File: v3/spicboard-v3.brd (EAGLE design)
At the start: 100 x 80 mm, 39 parts, among them IC1 74HC595N, Q1 BC557, Q2 BC557

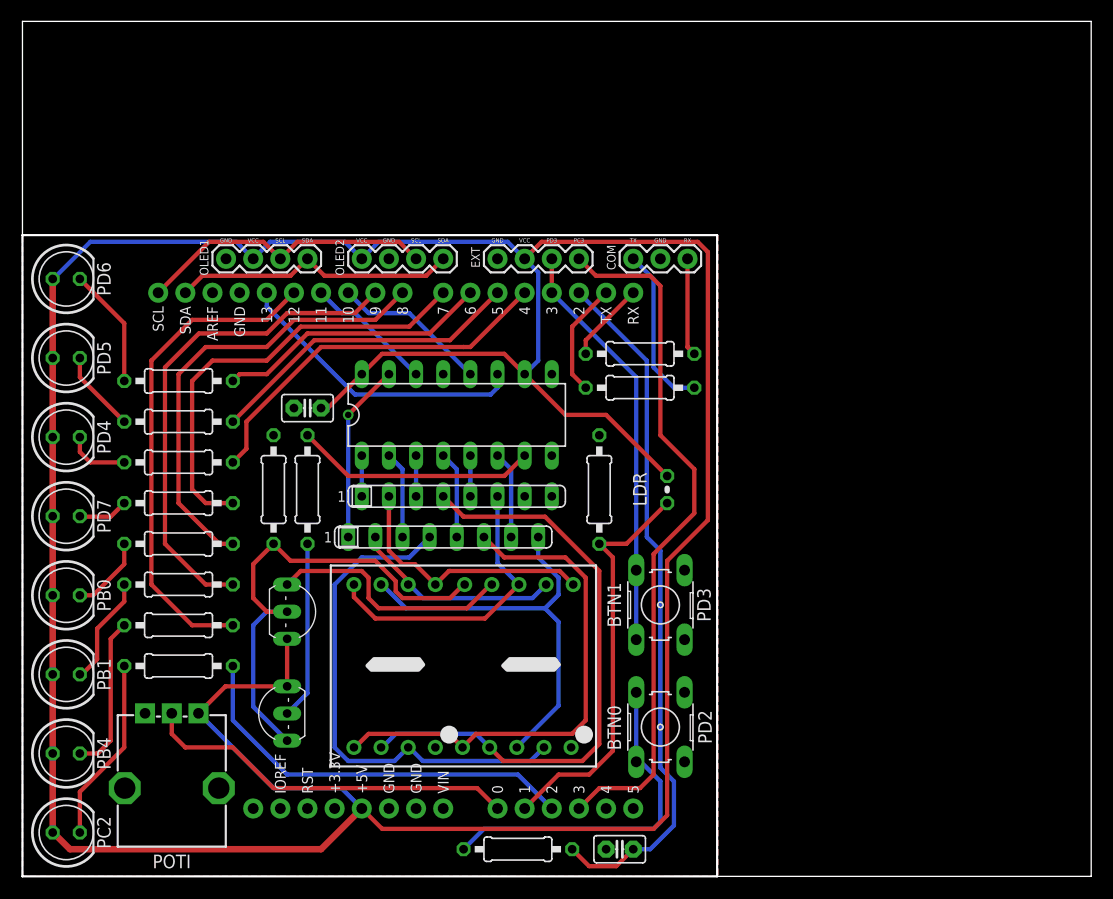
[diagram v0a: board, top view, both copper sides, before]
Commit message: SPiCboard: i4logo
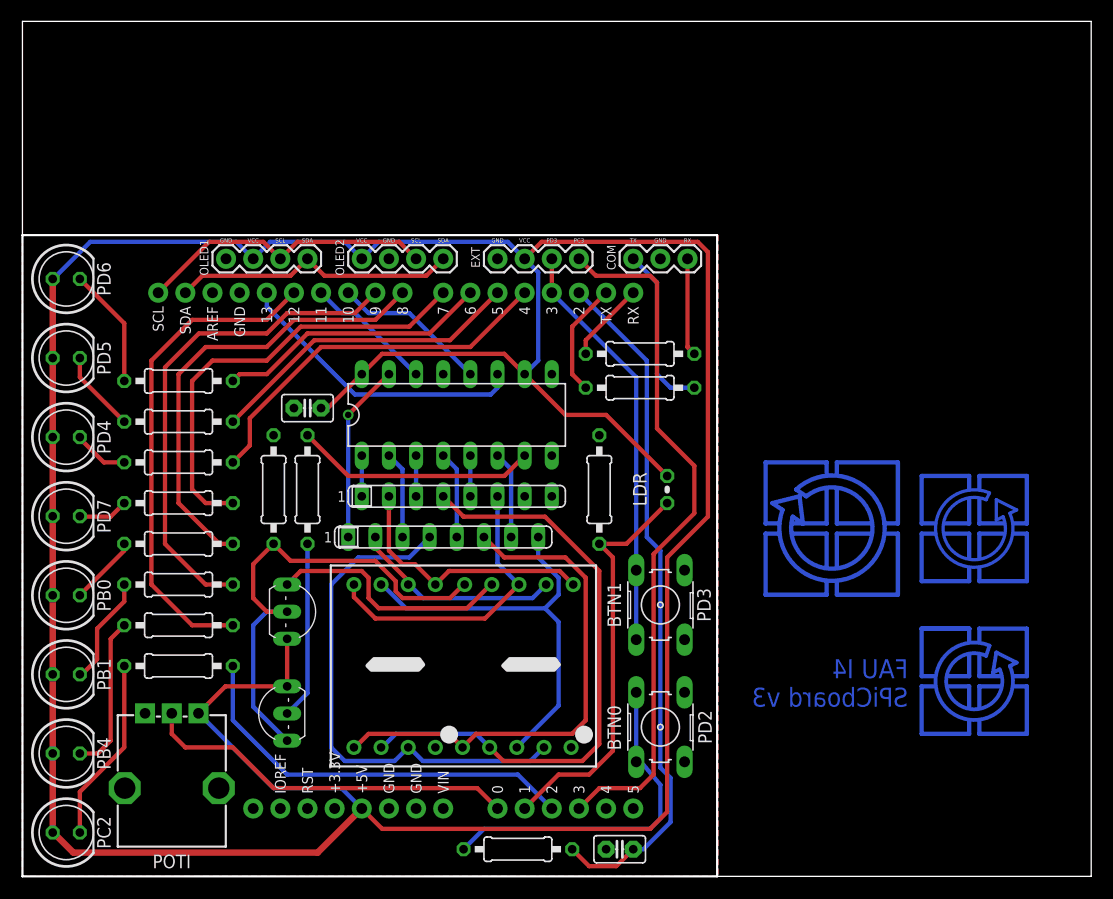
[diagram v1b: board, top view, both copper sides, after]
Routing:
- net NONE: track 0.00 -> 93.5 mm
- net N$30: track 0.00 -> 28.6 mm
- net N$26: track 0.00 -> 15.9 mm
- net N$23: track 0.00 -> 15.9 mm
- net N$33: track 0.00 -> 15.2 mm
- net N$25: track 0.00 -> 11.4 mm
- net N$32: track 0.00 -> 11.4 mm
- net N$24: track 0.00 -> 11.4 mm
- net N$31: track 0.00 -> 11.4 mm
- net N$27: track 0.00 -> 11.1 mm
- net N$34: track 0.00 -> 9.18 mm
- net N$29: track 0.00 -> 4.45 mm
- net N$28: track 0.00 -> 4.45 mm
- net N$36: track 0.00 -> 3.81 mm
- net N$35: track 0.00 -> 3.81 mm
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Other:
- board text added: "FAU I4 SPiCboard v3"

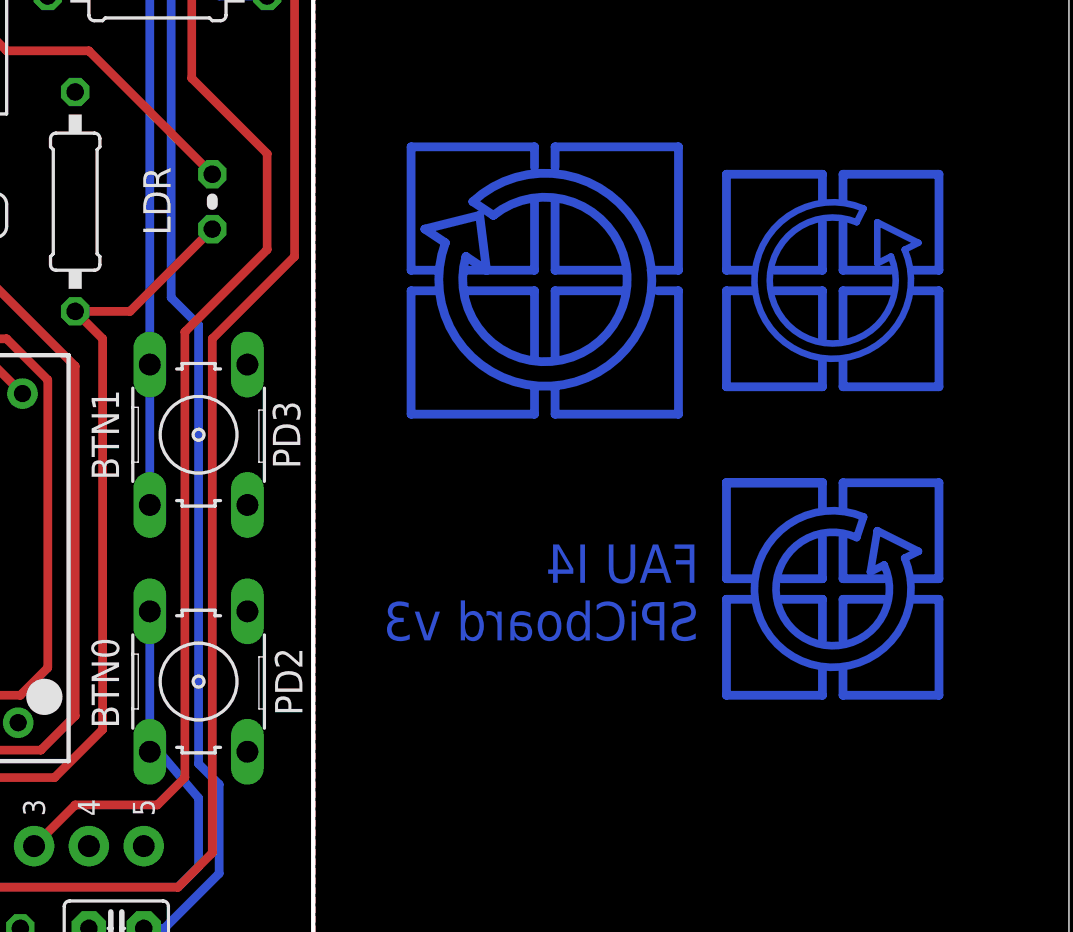
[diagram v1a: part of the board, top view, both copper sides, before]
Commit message: SPiCboard: i4logo, LDR -> PHOTO, TODOs aktualisiert
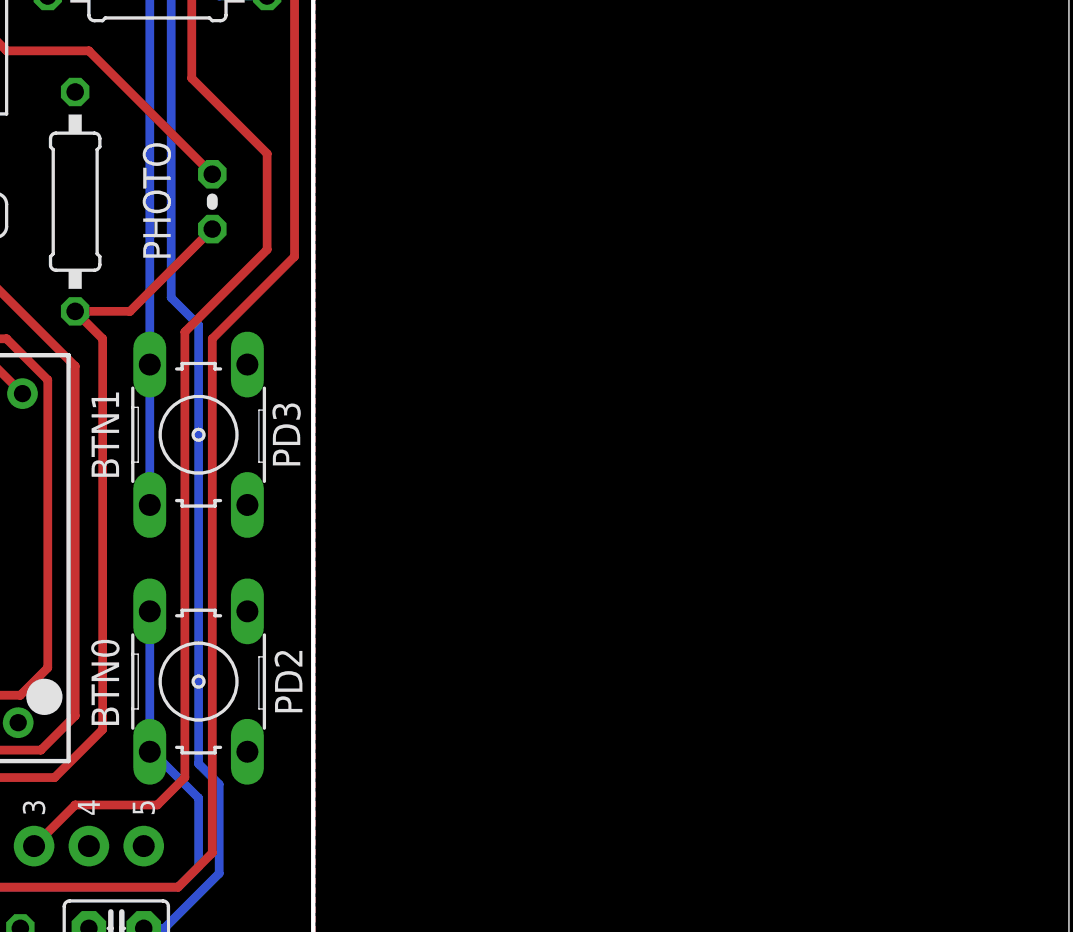
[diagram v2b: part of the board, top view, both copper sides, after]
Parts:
- renumbered LDR to PHOTO
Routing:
- net NONE: track 93.5 -> 0.00 mm
- net N$30: track 28.6 -> 0.00 mm
- net N$26: track 15.9 -> 0.00 mm
- net N$23: track 15.9 -> 0.00 mm
- net N$33: track 15.2 -> 0.00 mm
- net N$25: track 11.4 -> 0.00 mm
- net N$32: track 11.4 -> 0.00 mm
- net N$24: track 11.4 -> 0.00 mm
- net N$31: track 11.4 -> 0.00 mm
- net N$27: track 11.1 -> 0.00 mm
- net N$34: track 9.18 -> 0.00 mm
- net N$29: track 4.45 -> 0.00 mm
- net N$28: track 4.45 -> 0.00 mm
- net N$36: track 3.81 -> 0.00 mm
- net N$35: track 3.81 -> 0.00 mm
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
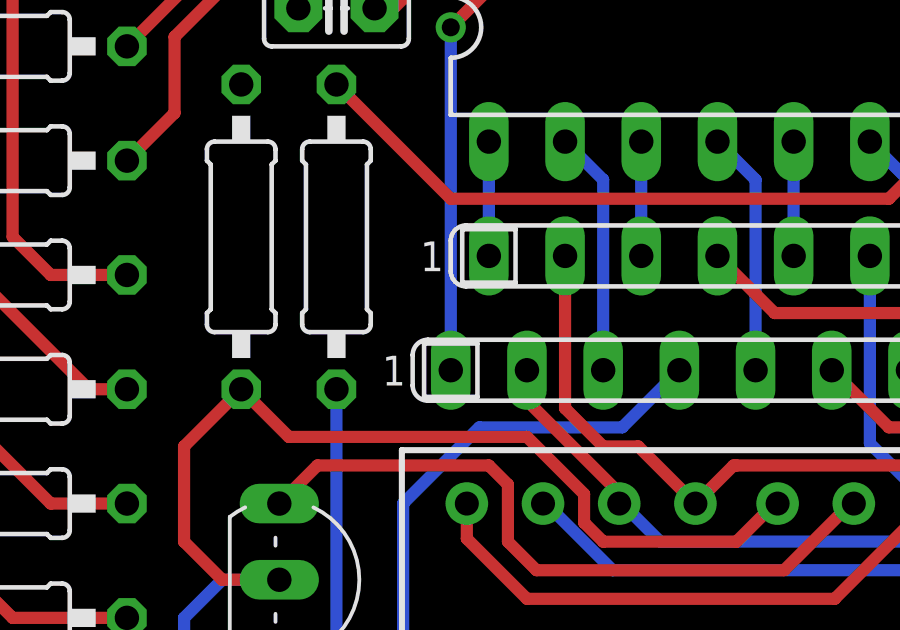
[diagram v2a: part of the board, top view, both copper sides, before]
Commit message: SPiCboard: Markierung am Widerstandsnetzwerk entfernt
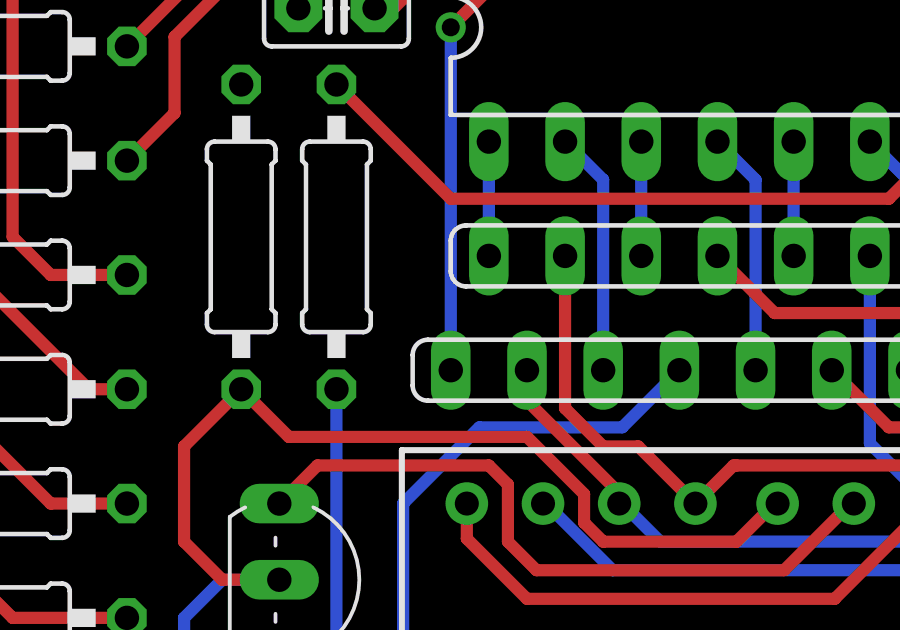
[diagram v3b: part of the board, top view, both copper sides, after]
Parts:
- RN1, RN2: device resistor-sil:SIL8 -> spicboard-v3:SIL8
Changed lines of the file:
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@@
 <attribute name="VALUE" x="13.97" y="3.556" size="1.27" layer="27" ratio="20" rot="R180" align="top-center"/>
 </element>
-<element name="RN1" library="resistor-sil" package="SIL8" value="330" x="40.64" y="35.56" smashed="yes">
+<element name="RN1" library="spicboard-v3" package="SIL8" value="330" x="40.64" y="35.56" smashed="yes">
 <attribute name="MPN" value="" x="40.64" y="35.56" size="1.778" layer="27" display="off"/>
 <attribute name="OC_FARNELL" value="unknown" x="40.64" y="35.56" size="1.778" layer="27" display="off"/>
@@
 <attribute name="VALUE" x="32.385" y="36.83" size="1.27" layer="27" ratio="10"/>
 </element>
-<element name="RN2" library="resistor-sil" package="SIL8" value="330" x="39.37" y="31.75" smashed="yes">
+<element name="RN2" library="spicboard-v3" package="SIL8" value="330" x="39.37" y="31.75" smashed="yes">
 <attribute name="MPN" value="" x="39.37" y="31.75" size="1.778" layer="27" display="off"/>
 <attribute name="OC_FARNELL" value="unknown" x="39.37" y="31.75" size="1.778" layer="27" display="off"/>

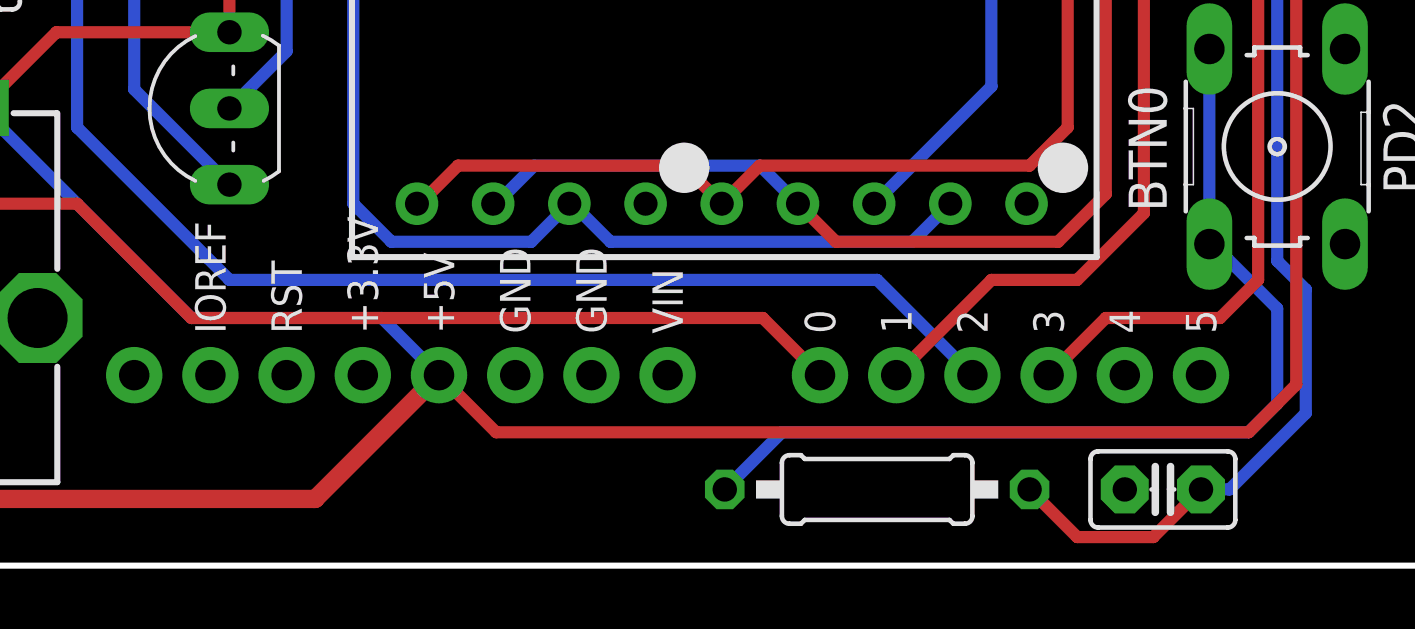
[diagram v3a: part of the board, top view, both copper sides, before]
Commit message: SPiCboard: Beschriftung verschoben
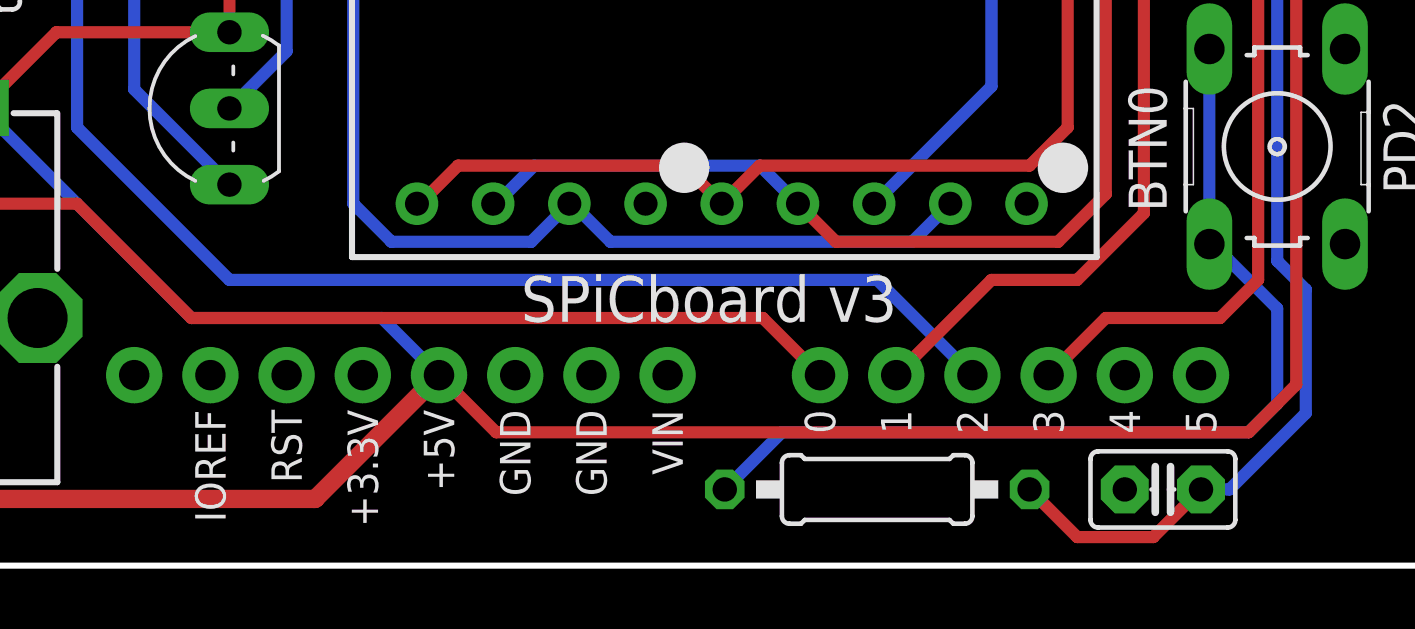
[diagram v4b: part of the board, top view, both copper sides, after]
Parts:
- B1: value ARDUINO_UNO_R3_SHIELDSPICBOARD_NOFRAME -> ARDUINO_UNO_R3_SHIELD; device spicboard-v3:UNO_R3_SHIELD_NOFRAME -> spicboard-v3:UNO_R3_SHIELD_FINAL
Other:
- board text added: "SPiCboard v3"
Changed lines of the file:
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@@
 <wire x1="48.895" y1="24.765" x2="48.895" y2="23.495" width="0.4064" layer="52"/>
 <wire x1="48.895" y1="20.32" x2="48.895" y2="22.225" width="0.4064" layer="52"/>
+<text x="34.4805" y="8.128" size="1.524" layer="25">SPiCboard v3</text>
 </plain>
 <attributes>
@@
 </autorouter>
 <elements>
-<element name="B1" library="spicboard-v3" package="UNO_R3_SHIELD_NOFRAME" value="ARDUINO_UNO_R3_SHIELDSPICBOARD_NOFRAME" x="24.13" y="35.56"/>
+<element name="B1" library="spicboard-v3" package="UNO_R3_SHIELD_FINAL" value="ARDUINO_UNO_R3_SHIELD" x="24.13" y="35.56"/>
 <element name="BLUE0" library="led" package="LED5MM" value="" x="4.1" y="33.7" smashed="yes">
 <attribute name="VALUE" x="7.3004" y="31.8966" size="1.27" layer="27" ratio="10"/>

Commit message: SPiCboard: Kleine Änderungen
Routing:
- net N$21: track 10.1 -> 9.15 mm
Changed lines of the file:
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@@
 <contactref element="POTI" pad="P$2"/>
 <contactref element="B1" pad="A0"/>
-<wire x1="13.97" y1="15.255" x2="13.97" y2="13.335" width="0.4064" layer="1"/>
-<wire x1="13.97" y1="13.335" x2="15.24" y2="12.065" width="0.4064" layer="1"/>
-<wire x1="15.24" y1="12.065" x2="19.685" y2="12.065" width="0.4064" layer="1"/>
+<wire x1="13.97" y1="15.255" x2="13.97" y2="13.6525" width="0.4064" layer="1"/>
+<wire x1="13.97" y1="13.6525" x2="15.5575" y2="12.065" width="0.4064" layer="1"/>
+<wire x1="15.5575" y1="12.065" x2="19.685" y2="12.065" width="0.4064" layer="1"/>
 <wire x1="19.685" y1="12.065" x2="23.495" y2="8.255" width="0.4064" layer="1"/>
 <wire x1="23.495" y1="8.255" x2="42.545" y2="8.255" width="0.4064" layer="1"/>
@@
 <signal name="L3">
 <contactref element="R4" pad="2"/>
-<wire x1="19.685" y1="34.925" x2="17.145" y2="34.925" width="0.4064" layer="1"/>
-<wire x1="17.145" y1="34.925" x2="15.875" y2="36.195" width="0.4064" layer="1"/>
-<wire x1="15.875" y1="36.195" x2="15.875" y2="46.355" width="0.4064" layer="1"/>
+<wire x1="19.685" y1="34.925" x2="17.78" y2="34.925" width="0.4064" layer="1"/>
+<wire x1="17.78" y1="34.925" x2="15.875" y2="36.83" width="0.4064" layer="1"/>
+<wire x1="15.875" y1="36.83" x2="15.875" y2="46.355" width="0.4064" layer="1"/>
 <wire x1="15.875" y1="46.355" x2="17.78" y2="48.26" width="0.4064" layer="1"/>
 <wire x1="17.78" y1="48.26" x2="22.86" y2="48.26" width="0.4064" layer="1"/>
@@
 <contactref element="R5" pad="2"/>
 <contactref element="B1" pad="D8"/>
-<wire x1="19.685" y1="31.115" x2="18.415" y2="31.115" width="0.4064" layer="1"/>
-<wire x1="18.415" y1="31.115" x2="14.605" y2="34.925" width="0.4064" layer="1"/>
-<wire x1="14.605" y1="34.925" x2="14.605" y2="46.99" width="0.4064" layer="1"/>
+<wire x1="19.685" y1="31.115" x2="17.78" y2="31.115" width="0.4064" layer="1"/>
+<wire x1="17.78" y1="31.115" x2="14.605" y2="34.29" width="0.4064" layer="1"/>
+<wire x1="14.605" y1="34.29" x2="14.605" y2="46.99" width="0.4064" layer="1"/>
 <wire x1="14.605" y1="46.99" x2="17.145" y2="49.53" width="0.4064" layer="1"/>
 <wire x1="17.145" y1="49.53" x2="22.86" y2="49.53" width="0.4064" layer="1"/>
@@
 <contactref element="R6" pad="2"/>
 <contactref element="B1" pad="D9"/>
-<wire x1="19.685" y1="27.305" x2="17.145" y2="27.305" width="0.4064" layer="1"/>
-<wire x1="17.145" y1="27.305" x2="13.335" y2="31.115" width="0.4064" layer="1"/>
-<wire x1="13.335" y1="31.115" x2="13.335" y2="47.625" width="0.4064" layer="1"/>
+<wire x1="19.685" y1="27.305" x2="17.78" y2="27.305" width="0.4064" layer="1"/>
+<wire x1="17.78" y1="27.305" x2="13.335" y2="31.75" width="0.4064" layer="1"/>
+<wire x1="13.335" y1="31.75" x2="13.335" y2="47.625" width="0.4064" layer="1"/>
 <wire x1="13.335" y1="47.625" x2="16.51" y2="50.8" width="0.4064" layer="1"/>
 <wire x1="16.51" y1="50.8" x2="22.86" y2="50.8" width="0.4064" layer="1"/>
@@
 <contactref element="R7" pad="2"/>
 <contactref element="B1" pad="D12"/>
-<wire x1="19.685" y1="23.495" x2="15.875" y2="23.495" width="0.4064" layer="1"/>
-<wire x1="15.875" y1="23.495" x2="12.065" y2="27.305" width="0.4064" layer="1"/>
-<wire x1="12.065" y1="27.305" x2="12.065" y2="48.26" width="0.4064" layer="1"/>
+<wire x1="19.685" y1="23.495" x2="16.51" y2="23.495" width="0.4064" layer="1"/>
+<wire x1="16.51" y1="23.495" x2="12.065" y2="27.94" width="0.4064" layer="1"/>
+<wire x1="12.065" y1="27.94" x2="12.065" y2="48.26" width="0.4064" layer="1"/>
 <wire x1="12.065" y1="48.26" x2="15.875" y2="52.07" width="0.4064" layer="1"/>
 <wire x1="15.875" y1="52.07" x2="22.86" y2="52.07" width="0.4064" layer="1"/>
@@
 <signal name="N$21">
 <contactref element="R13" pad="2"/>
-<wire x1="62.865" y1="48.895" x2="62.23" y2="49.53" width="0.4064" layer="1"/>
 <contactref element="COM" pad="3"/>
-<wire x1="62.865" y1="48.895" x2="62.23" y2="49.53" width="0.4064" layer="1"/>
-<wire x1="62.23" y1="49.53" x2="62.23" y2="57.785" width="0.4064" layer="1"/>
+<wire x1="62.23" y1="57.785" x2="62.865" y2="57.15" width="0.4064" layer="1"/>
+<wire x1="62.865" y1="57.15" x2="62.865" y2="48.895" width="0.4064" layer="1"/>
 </signal>
 <signal name="SS">
